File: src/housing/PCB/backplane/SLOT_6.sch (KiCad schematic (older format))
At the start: 1 part, among them J4 10018784-10201TLF

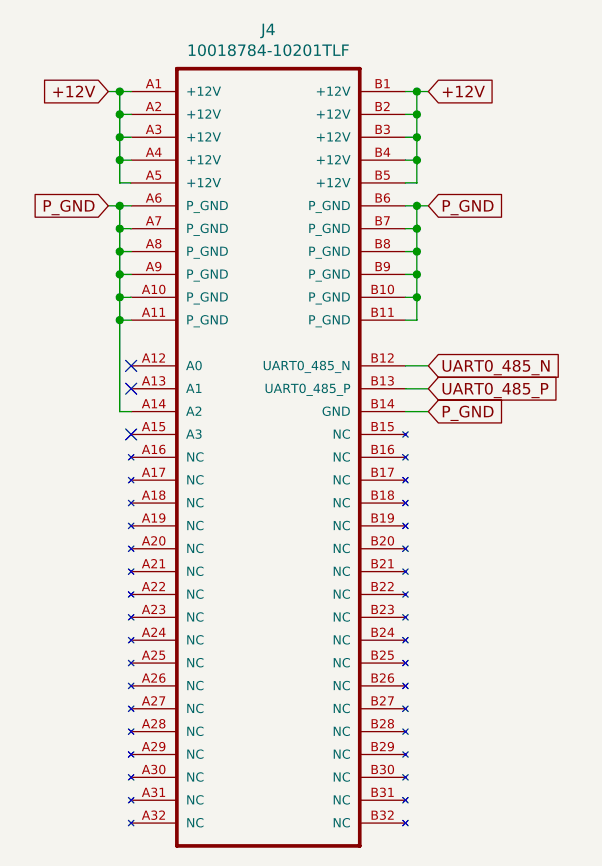
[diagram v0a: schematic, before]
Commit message: fixing backplane libraries path error
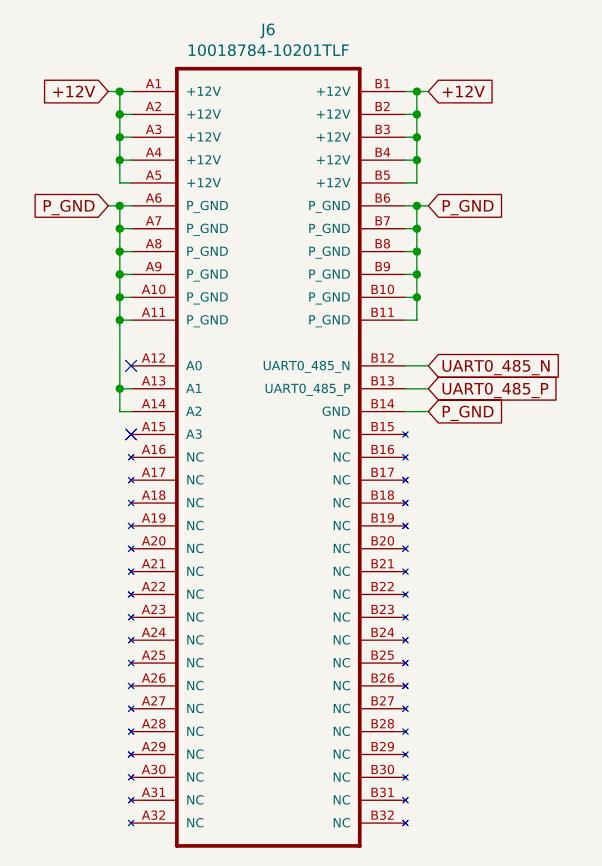
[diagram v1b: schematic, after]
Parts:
- removed J4: 10018784-10201TLF, kicad-lib:CONN_10018784-10201TLF, symbol 10018784-10201TLF:10018784-10201TLF
- added J6: 10018784-10201TLF, kicad-lib:CONN_10018784-10201TLF, symbol 10018784-10201TLF:10018784-10201TLF
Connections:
- net +12V: now also J6.A1 (+12V), J6.A2 (+12V), J6.A3 (+12V), J6.A4 (+12V), J6.A5 (+12V), J6.B1 (+12V), J6.B2 (+12V), J6.B3 (+12V), J6.B4 (+12V), J6.B5 (+12V)
- net P_GND: now also J6.A10 (P_GND), J6.A11 (P_GND), J6.A13 (A1), J6.A14 (A2), J6.A6 (P_GND), J6.A7 (P_GND), J6.A8 (P_GND), J6.A9 (P_GND), J6.B10 (P_GND), J6.B11 (P_GND), J6.B14 (GND), J6.B6 (P_GND), J6.B7 (P_GND), J6.B8 (P_GND), J6.B9 (P_GND)
- net UART0_485_N: now also J6.B12 (UART0_485_N)
- net UART0_485_P: now also J6.B13 (UART0_485_P)
- no-connect marks 3 -> 2
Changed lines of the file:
@@
 $Descr A4 11693 8268
 encoding utf-8
-Sheet 5 9
-Title ""
+Sheet 7 9
+Title "ACS backplane"
 Date ""
-Rev ""
-Comp ""
-Comment1 ""
+Rev "1"
+Comp "Halidelabs"
+Comment1 "contact@halidelabs.eu"
 Comment2 ""
 Comment3 ""
@@
 $Comp
 L 10018784-10201TLF:10018784-10201TLF J?
-U 1 1 5DF52F0E
+U 1 1 5DF52F0C
 P 5600 3950
-AR Path="/5DF19C0C/5DF52F0E" Ref="J?"  Part="1"
-AR Path="/5DF2A71E/5DF52F0E" Ref="J?"  Part="1"
-AR Path="/5DF2E10A/5DF52F0E" Ref="J?"  Part="1"
-AR Path="/5DF2E1F8/5DF52F0E" Ref="J4"  Part="1"
-AR Path="/5DF2E248/5DF52F0E" Ref="J?"  Part="1"
-AR Path="/5DF2E24C/5DF52F0E" Ref="J?"  Part="1"
-F 0 "J4" H 5600 5820 50  0000 C CNN
+AR Path="/5DF19C0C/5DF52F0C" Ref="J?"  Part="1"
+AR Path="/5DF2A71E/5DF52F0C" Ref="J?"  Part="1"
+AR Path="/5DF2E10A/5DF52F0C" Ref="J?"  Part="1"
+AR Path="/5DF2E1F8/5DF52F0C" Ref="J?"  Part="1"
+AR Path="/5DF2E248/5DF52F0C" Ref="J6"  Part="1"
+AR Path="/5DF2E24C/5DF52F0C" Ref="J?"  Part="1"
+F 0 "J6" H 5600 5820 50  0000 C CNN
 F 1 "10018784-10201TLF" H 5600 5729 50  0000 C CNN
 F 2 "kicad-lib:CONN_10018784-10201TLF" H 5650 4450 50  0001 L BNN
@@
 Connection ~ 4950 3350
 Wire Wire Line
+	4950 3650 5000 3650
+Wire Wire Line
+	4950 3350 4950 3650
+Wire Wire Line
+	4950 3650 4950 3750
+Wire Wire Line
 	4950 3750 5000 3750
-Wire Wire Line
-	4950 3350 4950 3750
+Connection ~ 4950 3650
 NoConn ~ 5000 3550
-NoConn ~ 5000 3650
 NoConn ~ 5000 3850
 $EndSCHEMATC
